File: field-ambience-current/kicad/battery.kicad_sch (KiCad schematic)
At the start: 24 parts, among them J9 JST PH 2.0 2-pin (LiPo Batter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, U7 MCP73831T-2ACI/OT (LiPo Charg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, U8 TPS61089RNR (Boost LiPo→5V, 2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

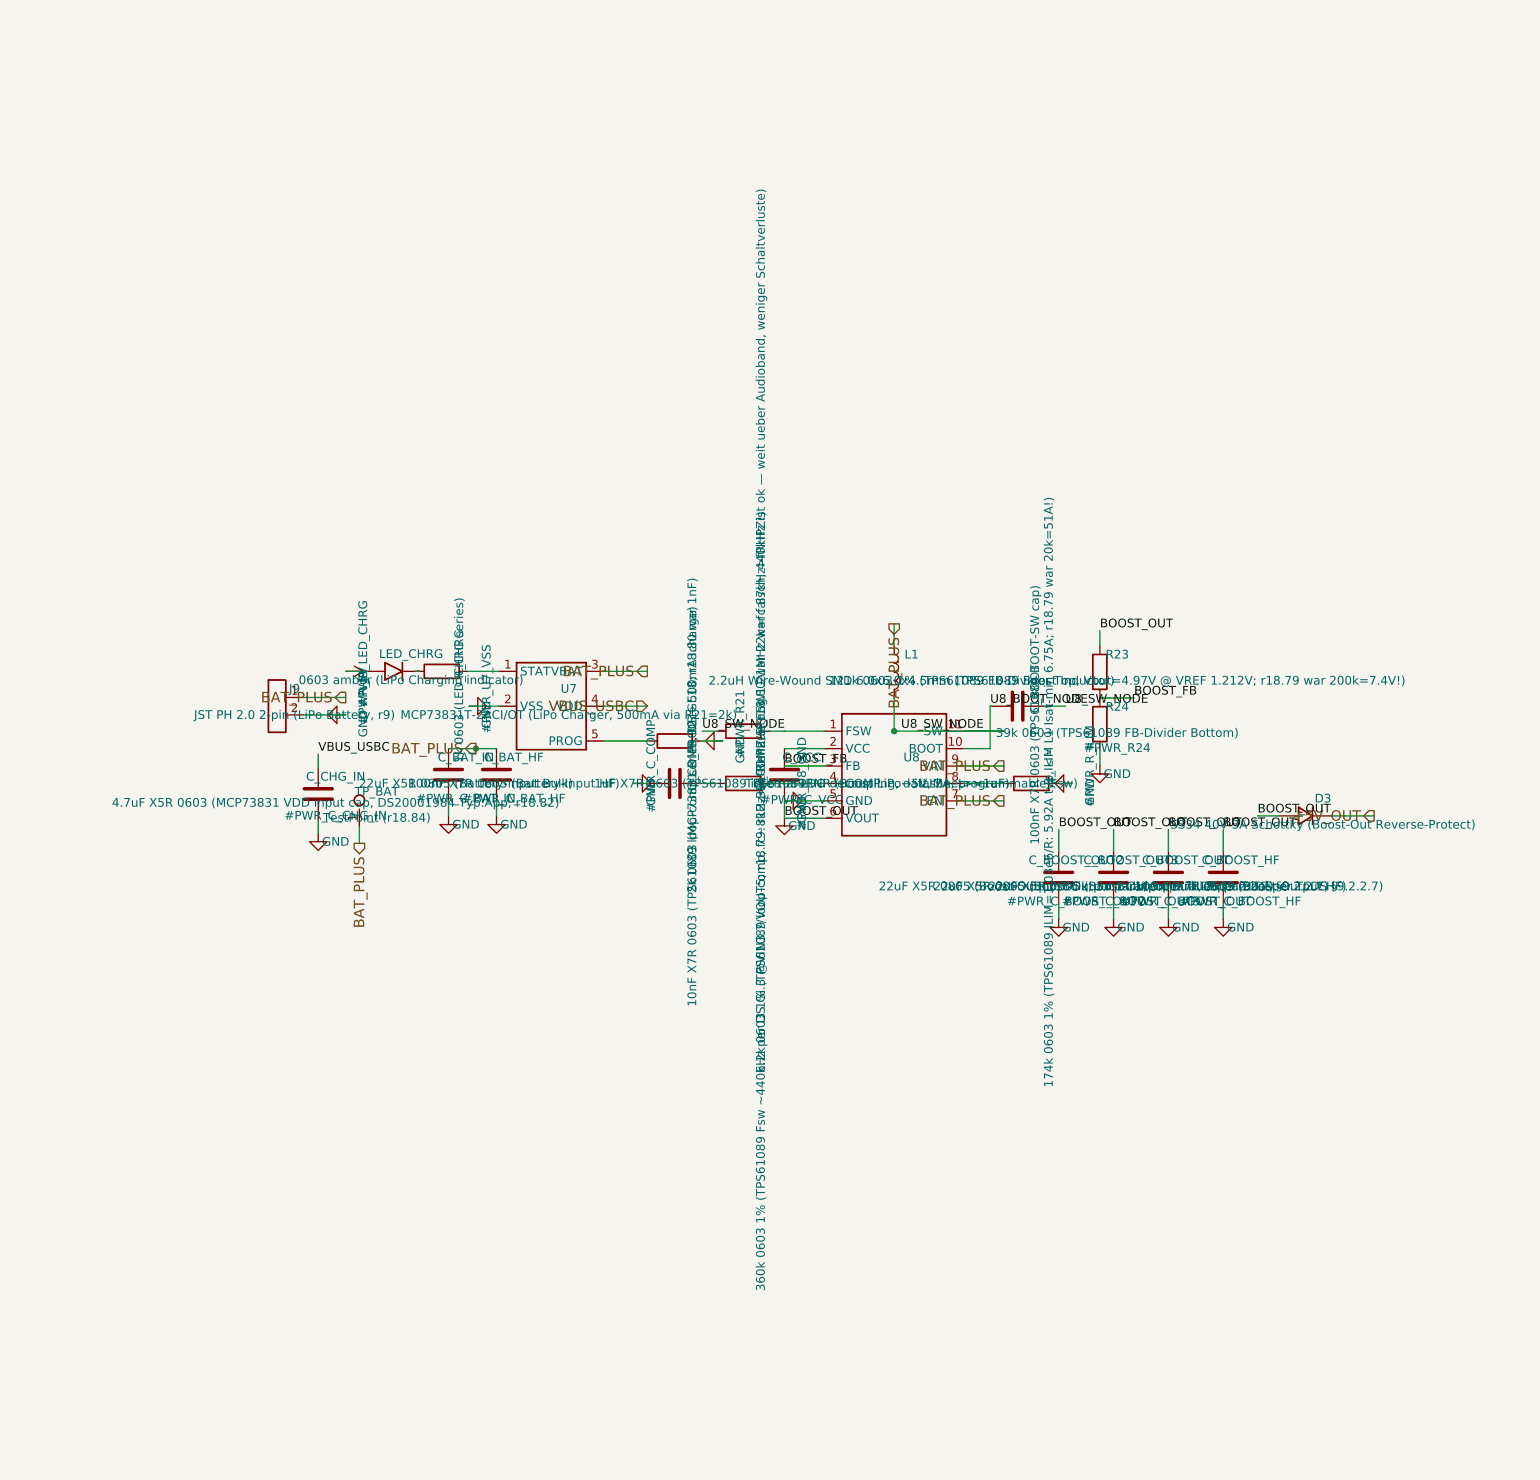
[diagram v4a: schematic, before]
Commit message: feat(hw): BQ24074 power-path replaces MCP73831 + diode-OR — all audit P0 fixed (r19.18, ADR-0023)
External hardware audit verdict was DO NOT FABRICATE; every checkable P0
was confirmed against the extracted netlist, then fixed at the generator:

- U7 = BQ24074RGTR (C54313, live-verified stock + JLC assembly):
  USB->F1->VBUS_FUSED->IN; OUT=VSYS->TPS61089->D3->+5V rail (single
  source, D3B diode-OR deleted); BAT<-F2 PTC (SMD1812P260TF/16,
  C438899)<-J9. Values per TI SLUS810N: ICHG 0.89A (R_ISET 1k),
  IIN 1.34A (R_ILIM_IN 1.2k YAGEO C114605), ITERM/TMR=NC defaults,
  TS=10k fixed, EN2=VSYS/EN1=GND, CE_N=GND, EP->VSS.
- Boost EN = PWR_ON (was always-on battery drain); SW_PWR pull source
  moved to VSYS (rail-sourced pull would deadlock); LED_CHRG now fed
  from VBUS_FUSED via CHG open-drain; rail bulk sits behind the boost
  (USB hot-plug sees only 4.7uF).
- New inter-sheet nets VBUS_FUSED/VSYS/PWR_ON via root; +5V_OUT is now
  an input on the power tree. TP_VSYS test point added.
- Footprint QFN-16-1EP_3x3mm_P0.5mm_EP1.7x1.7mm matched against the
  JLC/EasyEDA land pattern for C54313 (pitch/pads/EP identical).
- J4 SWD = DNP debug pads (bogus TC2030-IDC MPN + LCSC "TBD" removed
  from the order BOM); J8 explicitly LINE OUT; mechanical doc battery
  corrected 5000->2000 mAh.
- Validation: geometric netlist extractor over all 7 sheets — 157 nets,
  620 pins, 0 floating; check_pinmap green; host suite green (32 suites).
- Docs: ADR-0023, CHANGELOG r19.18, PROJECT_STATUS banner, SCHEMATIC_
  WALKTHROUGH §1/§7 rewritten, PINMAP/BRING_UP/BOM_MASTER/PCB_BOM/
  COST/SOURCING/OBJECTIVES/COMPONENT_LINKS/FOOTPRINT_RISK updated.

Co-Authored-By: Claude Fable 5 <noreply@anthropic.com>
Claude-Session: https://claude.ai/code/session_019pKguH6aG4iazMCWJnpmMn
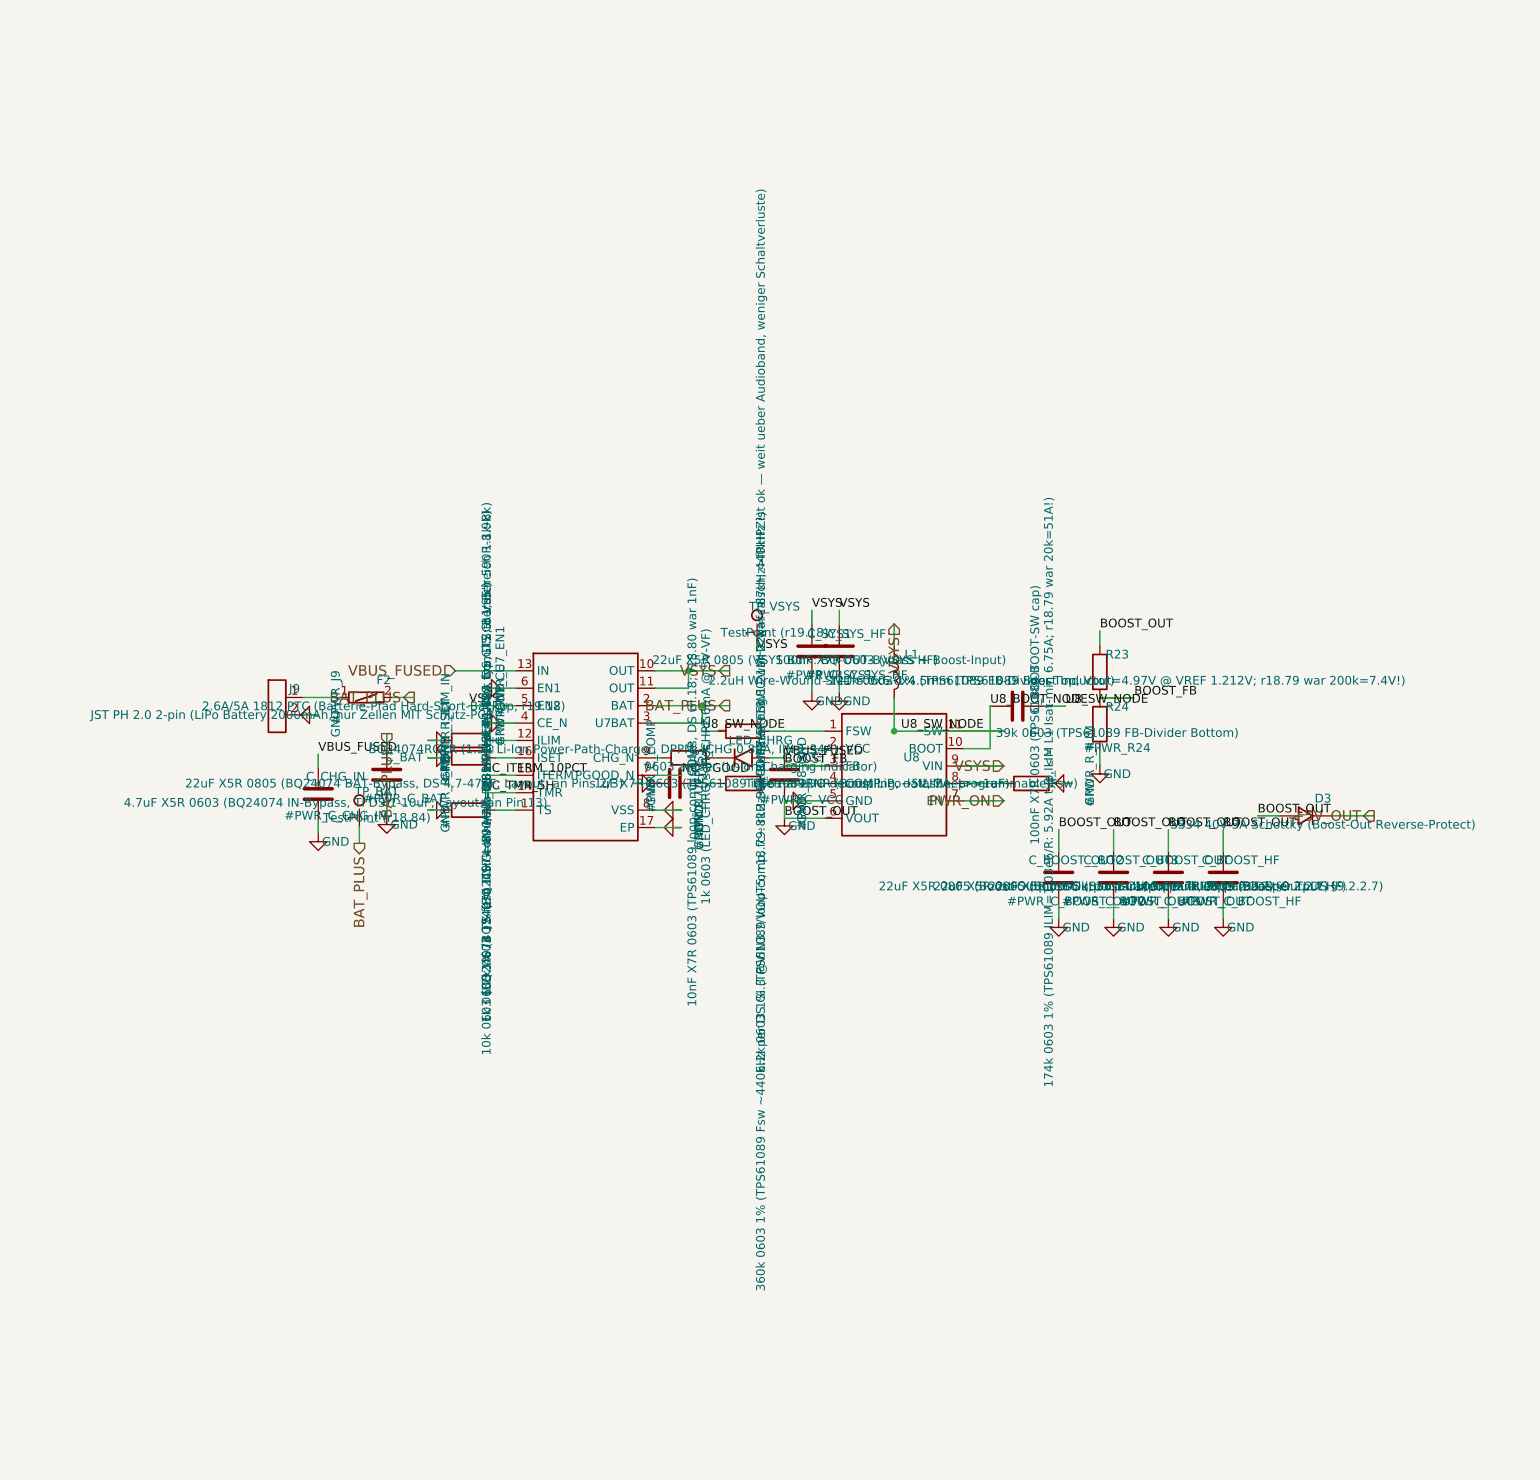
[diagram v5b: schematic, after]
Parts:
- removed C_BAT_HF: 100nF X7R 0603 (Battery-Input HF), Capacitor_SMD:C_0603_1608Metric, symbol Device:C
- removed C_BAT_IN: 22uF X5R 0805 (Battery-Input Bulk), Capacitor_SMD:C_0805_2012Metric, symbol Device:C
- removed R21: 2k 0603 (MCP73831 R_PROG → 500mA Icharge), Resistor_SMD:R_0603_1608Metric, symbol Device:R
- added C_BAT: 22uF X5R 0805 (BQ24074 BAT-Bypass, DS 4.7-47uF; L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, Capacitor_SMD:C_0805_2012Metric, symbol Device:C
- added C_SYS1: 22uF X5R 0805 (VSYS Bulk: BQ-OUT-Bypass + Boost-I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, Capacitor_SMD:C_0805_2012Metric, symbol Device:C
- added C_SYS_HF: 100nF X7R 0603 (VSYS HF), Capacitor_SMD:C_0603_1608Metric, symbol Device:C
- added F2: 2.6A/5A 1812 PTC (Batterie-Pfad Hard-Short-Backup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, Fuse:Fuse_1812_4532Metric, symbol Device:Polyfuse
- added R_ILIM_IN: 1.2k 0603 1% (BQ24074 IIN-MAX=1610/1.2k=1.34A typ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, Resistor_SMD:R_0603_1608Metric, symbol Device:R
- added R_ISET: 1k 0603 1% (BQ24074 ICHG=890/1k=0.89A typ ≈0.45C,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, Resistor_SMD:R_0603_1608Metric, symbol Device:R
- added R_TS: 10k 0603 (BQ24074 TS fest, DS: 'connect a 10-k fi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, Resistor_SMD:R_0603_1608Metric, symbol Device:R
- added TP_VSYS: TestPoint (r19.18), TestPoint:TestPoint_Pad_D1.5mm, symbol Connector:TestPoint
- C_CHG_IN: value 4.7uF X5R 0603 (MCP73831 VDD input cap, DS20001984 Typ.App; r18.82) -> 4.7uF X5R 0603 (BQ24074 IN-Bypass, TI DS 1-10uF; Layout: an Pin 13)
- J9: value JST PH 2.0 2-pin (LiPo Battery, r9) -> JST PH 2.0 2-pin (LiPo Battery 2000mAh, nur Zellen MIT Schutz-PCB); NOTE (none) -> Kontakt-Rating 2A/Pin — Peak-Transienten reiten die VSYS/Bo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
- LED_CHRG: value 0603 amber (LiPo Charging indicator) -> 0603 amber (Li-Ion Charging indicator)
- R_CHRG: value 1k 0603 (LED_CHRG series) -> 1k 0603 (LED_CHRG series, ~2.6mA @ 5V-VF)
- U7: value MCP73831T-2ACI/OT (LiPo Charger, 500mA via R21=2k) -> BQ24074RGTR (1.5A Li-Ion Power-Path-Charger, DPPM; ICHG 0.89A, IIN 1.34A); footprint Package_TO_SOT_SMD:SOT-23-5 -> Package_DFN_QFN:QFN-16-1EP_3x3mm_P0.5mm_EP1.7x1.7mm; symbol Battery:MCP73831 -> Battery:BQ24074; FP_NOTE (none) -> KiCad-Standard QFN-16-1EP_3x3mm_P0.5mm_EP1.7x1.7mm — gegen 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; LCSC C424093 -> C54313; MPN MCP73831T-2ACI/OT -> BQ24074RGTR; Manufacturer (none) -> Texas Instruments; NOTE (none) -> r19.18 live-verifiziert: LCSC C54313, 1.074 Stk., $2.24@1/$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; PIN_SOURCE (none) -> TI SLUS810N (Okt 2021) Table 7-1 Pin Functions, Spalte '74: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; Package (none) -> VQFN-16 RGT0016B (3x3mm, 0.5mm Pitch, EP)
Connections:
- net BAT_PLUS: now also U7.2 (BAT), C_BAT.1, F2.2; no longer J9.1 (Pin_1), L1.1, U8.7 (EN), U8.9 (VIN)
- net GND: now also U7.17 (EP), U7.4 (CE_N), U7.6 (EN1), U7.8 (VSS), C_BAT.2, C_SYS1.2, C_SYS_HF.2, R_ILIM_IN.1, R_ISET.1, R_TS.1; no longer U7.2 (VSS)
- net VSYS: now reaches U7.5 (EN2)
- net VSYS: now also L1.1, U7.10 (OUT), U7.11 (OUT), U8.9 (VIN), C_SYS1.1, C_SYS_HF.1, TP_VSYS.1
- net at R_CHRG.1: now also U7.9 (CHG_N); no longer LED_CHRG.1 (K)
- net at U7.1 (TS): now also R_TS.2; no longer R_CHRG.2
- net +5V renamed VBUS_FUSED
- net VBUS_FUSED: now also C_CHG_IN.1, U7.13 (IN)
- removed net VBUS_USBC: C_CHG_IN.1, U7.4 (VDD)
- new net: F2.1, J9.1 (Pin_1)
- new net: LED_CHRG.1 (K), R_CHRG.2
- new net: R_ISET.2, U7.16 (ISET)
- new net: R_ILIM_IN.2, U7.12 (ILIM)
- new net NC_ITERM_10PCT: U7.15 (ITERM)
- new net NC_PGOOD: U7.7 (PGOOD_N)
- new net NC_TMR_5H: U7.14 (TMR)
- new net PWR_ON: U8.7 (EN)
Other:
- title: Field Ambience PCB — Sheet 7: Battery & Power-Path (r9 + r12) -> Field Ambience PCB — Sheet 7: Battery & Power-Path (r19.18 ADR-0023)
- moved on the sheet: LED_CHRG, R_CHRG
